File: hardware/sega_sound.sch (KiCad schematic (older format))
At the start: 12 parts, among them J1 Conn_01x02, J2 Conn_01x02, J3 AVR-ISP-6, U1 SN76489AN, U2 ATmega8-16PU

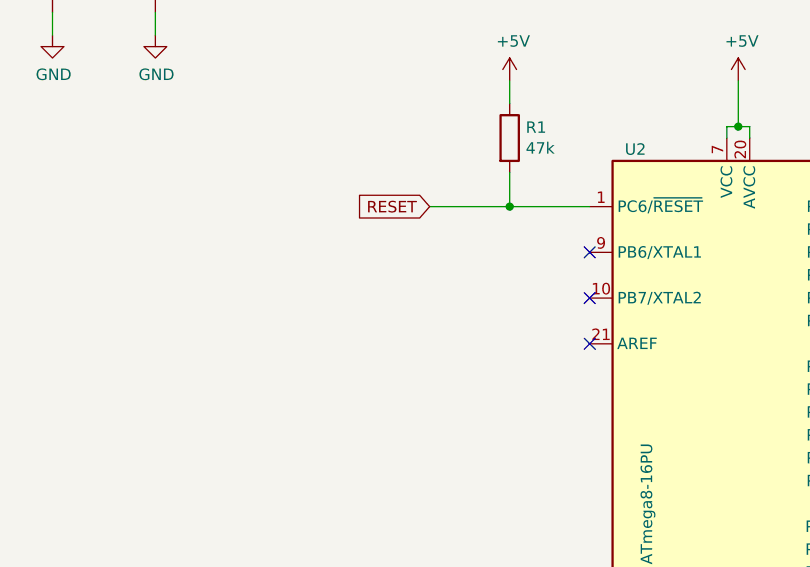
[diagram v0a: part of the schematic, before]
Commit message: hardware: added a 8MHz crystal with two 22pF capacitors
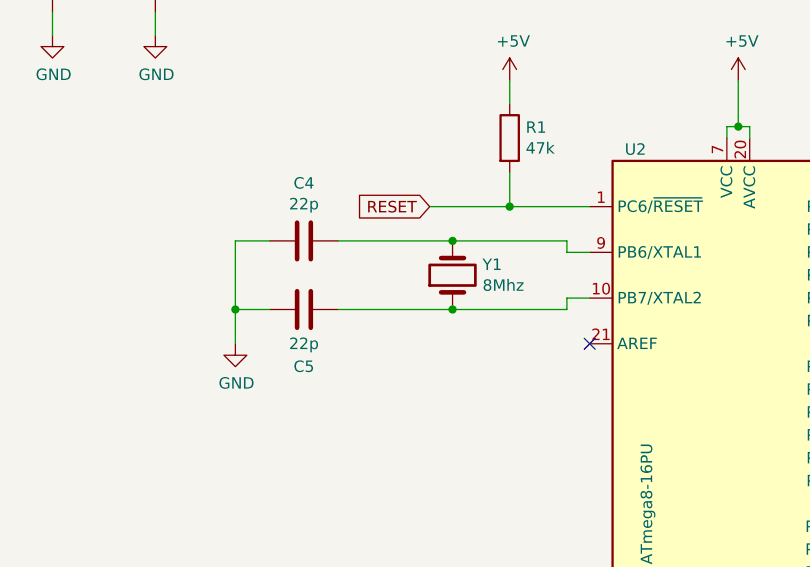
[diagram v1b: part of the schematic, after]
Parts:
- added C4, C5: 22p, symbol Device:C
- added Y1: 8Mhz, symbol Device:Crystal
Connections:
- net GND: now also C4.2, C5.2
- net at U2.10 (PB7/XTAL2): now also C5.1, Y1.1
- net at U2.9 (PB6/XTAL1): now also C4.1, Y1.2
- no-connect marks 7 -> 5
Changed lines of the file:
@@
 Sheet 1 2
 Title "Sega Sound with SN76489AN"
-Date "2020-02-05"
+Date "2020-02-07"
 Rev "1.0"
 Comp "Thorsten Kattanek"
@@
 $EndDescr
 $Comp
-L power:+5V #PWR09
+L power:+5V #PWR010
 U 1 1 5E271210
 P 8700 3550
-F 0 "#PWR09" H 8700 3400 50  0001 C CNN
+F 0 "#PWR010" H 8700 3400 50  0001 C CNN
 F 1 "+5V" H 8715 3723 50  0000 C CNN
 F 2 "" H 8700 3550 50  0001 C CNN
@@
 Connection ~ 4200 1850
 $Comp
-L power:GND #PWR012
+L power:GND #PWR013
 U 1 1 5E273378
 P 4200 4850
-F 0 "#PWR012" H 4200 4600 50  0001 C CNN
+F 0 "#PWR013" H 4200 4600 50  0001 C CNN
 F 1 "GND" H 4205 4677 50  0000 C CNN
 F 2 "" H 4200 4850 50  0001 C CNN
@@
 Connection ~ 4200 4750
 $Comp
-L power:GND #PWR010
+L power:GND #PWR011
 U 1 1 5E2743A8
 P 8700 3950
-F 0 "#PWR010" H 8700 3700 50  0001 C CNN
+F 0 "#PWR011" H 8700 3700 50  0001 C CNN
 F 1 "GND" H 8705 3777 50  0000 C CNN
 F 2 "" H 8700 3950 50  0001 C CNN
@@
 Connection ~ 3200 2200
 $Comp
-L power:+5V #PWR017
+L power:+5V #PWR018
 U 1 1 5E279685
 P 1750 6350
-F 0 "#PWR017" H 1750 6200 50  0001 C CNN
+F 0 "#PWR018" H 1750 6200 50  0001 C CNN
 F 1 "+5V" H 1765 6523 50  0000 C CNN
 F 2 "" H 1750 6350 50  0001 C CNN
@@
 $EndComp
 $Comp
-L power:GND #PWR019
+L power:GND #PWR020
 U 1 1 5E279E4E
 P 1750 7450
-F 0 "#PWR019" H 1750 7200 50  0001 C CNN
+F 0 "#PWR020" H 1750 7200 50  0001 C CNN
 F 1 "GND" H 1755 7277 50  0000 C CNN
 F 2 "" H 1750 7450 50  0001 C CNN
@@
 NoConn ~ 4750 3400
 NoConn ~ 3550 2800
-NoConn ~ 3550 2600
-NoConn ~ 3550 2400
 $Comp
 L Device:C C1
@@
 STATUS_LED
 $Comp
-L power:GND #PWR018
+L power:GND #PWR019
 U 1 1 5E29C499
 P 3100 7350
-F 0 "#PWR018" H 3100 7100 50  0001 C CNN
+F 0 "#PWR019" H 3100 7100 50  0001 C CNN
 F 1 "GND" H 3105 7177 50  0000 C CNN
 F 2 "" H 3100 7350 50  0001 C CNN
@@
 $EndComp
 $Comp
-L power:+5V #PWR011
+L power:+5V #PWR012
 U 1 1 5E3B7117
 P 7600 4450
-F 0 "#PWR011" H 7600 4300 50  0001 C CNN
+F 0 "#PWR012" H 7600 4300 50  0001 C CNN
 F 1 "+5V" H 7615 4623 50  0000 C CNN
 F 2 "" H 7600 4450 50  0001 C CNN
@@
 $EndComp
 $Comp
-L power:GND #PWR016
+L power:GND #PWR017
 U 1 1 5E3D1FA3
 P 8750 5950
-F 0 "#PWR016" H 8750 5700 50  0001 C CNN
+F 0 "#PWR017" H 8750 5700 50  0001 C CNN
 F 1 "GND" H 8755 5777 50  0000 C CNN
 F 2 "" H 8750 5950 50  0001 C CNN
@@
 $EndComp
 $Comp
-L power:GND #PWR015
+L power:GND #PWR016
 U 1 1 5E3D2F04
 P 7700 5950
-F 0 "#PWR015" H 7700 5700 50  0001 C CNN
+F 0 "#PWR016" H 7700 5700 50  0001 C CNN
 F 1 "GND" H 7705 5777 50  0000 C CNN
 F 2 "" H 7700 5950 50  0001 C CNN
@@
 	7700 5800 7700 5950
 $Comp
-L power:+12V #PWR014
+L power:+12V #PWR015
 U 1 1 5E3D615E
 P 8600 5900
-F 0 "#PWR014" H 8600 5750 50  0001 C CNN
+F 0 "#PWR015" H 8600 5750 50  0001 C CNN
 F 1 "+12V" V 8615 6028 50  0000 L CNN
 F 2 "" H 8600 5900 50  0001 C CNN
@@
 $EndComp
 $Comp
-L power:+5V #PWR013
+L power:+5V #PWR014
 U 1 1 5E3D8780
 P 7550 5900
-F 0 "#PWR013" H 7550 5750 50  0001 C CNN
+F 0 "#PWR014" H 7550 5750 50  0001 C CNN
 F 1 "+5V" H 7565 6073 50  0000 C CNN
 F 2 "" H 7550 5900 50  0001 C CNN
@@
 Text Notes 8400 5400 0    50   ~ 0
 12V Einspeisung
+$Comp
+L Device:Crystal Y1
+U 1 1 5E3DDB24
+P 2950 2500
+F 0 "Y1" V 2996 2369 50  0000 R CNN
+F 1 "8Mhz" V 2905 2369 50  0000 R CNN
+F 2 "" H 2950 2500 50  0001 C CNN
+F 3 "~" H 2950 2500 50  0001 C CNN
+	1    2950 2500
+	0    -1   -1   0
+$EndComp
+Wire Wire Line
+	2950 2350 3450 2350
+Wire Wire Line
+	3450 2350 3450 2400
+Wire Wire Line
+	3450 2400 3550 2400
+Wire Wire Line
+	2950 2650 3450 2650
+Wire Wire Line
+	3450 2650 3450 2600
+Wire Wire Line
+	3450 2600 3550 2600
+$Comp
+L Device:C C4
+U 1 1 5E3E5831
+P 2300 2350
+F 0 "C4" V 2048 2350 50  0000 C CNN
+F 1 "22p" V 2139 2350 50  0000 C CNN
+F 2 "" H 2338 2200 50  0001 C CNN
+F 3 "~" H 2300 2350 50  0001 C CNN
+	1    2300 2350
+	0    1    1    0
+$EndComp
+$Comp
+L Device:C C5
+U 1 1 5E3E6B19
+P 2300 2650
+F 0 "C5" V 2550 2650 50  0000 C CNN
+F 1 "22p" V 2450 2650 50  0000 C CNN
+F 2 "" H 2338 2500 50  0001 C CNN
+F 3 "~" H 2300 2650 50  0001 C CNN
+	1    2300 2650
+	0    1    1    0
+$EndComp
+Wire Wire Line
+	2450 2350 2950 2350
+Connection ~ 2950 2350
+Wire Wire Line
+	2450 2650 2950 2650
+Connection ~ 2950 2650
+$Comp
+L power:GND #PWR09
+U 1 1 5E3EB5E2
+P 2000 2800
+F 0 "#PWR09" H 2000 2550 50  0001 C CNN
+F 1 "GND" H 2005 2627 50  0000 C CNN
+F 2 "" H 2000 2800 50  0001 C CNN
+F 3 "" H 2000 2800 50  0001 C CNN
+	1    2000 2800
+	1    0    0    -1
+$EndComp
+Wire Wire Line
+	2000 2800 2000 2650
+Wire Wire Line
+	2000 2350 2150 2350
+Wire Wire Line
+	2150 2650 2000 2650
+Connection ~ 2000 2650
+Wire Wire Line
+	2000 2650 2000 2350
 $EndSCHEMATC
